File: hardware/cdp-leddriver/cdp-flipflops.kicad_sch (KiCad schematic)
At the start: 9 parts

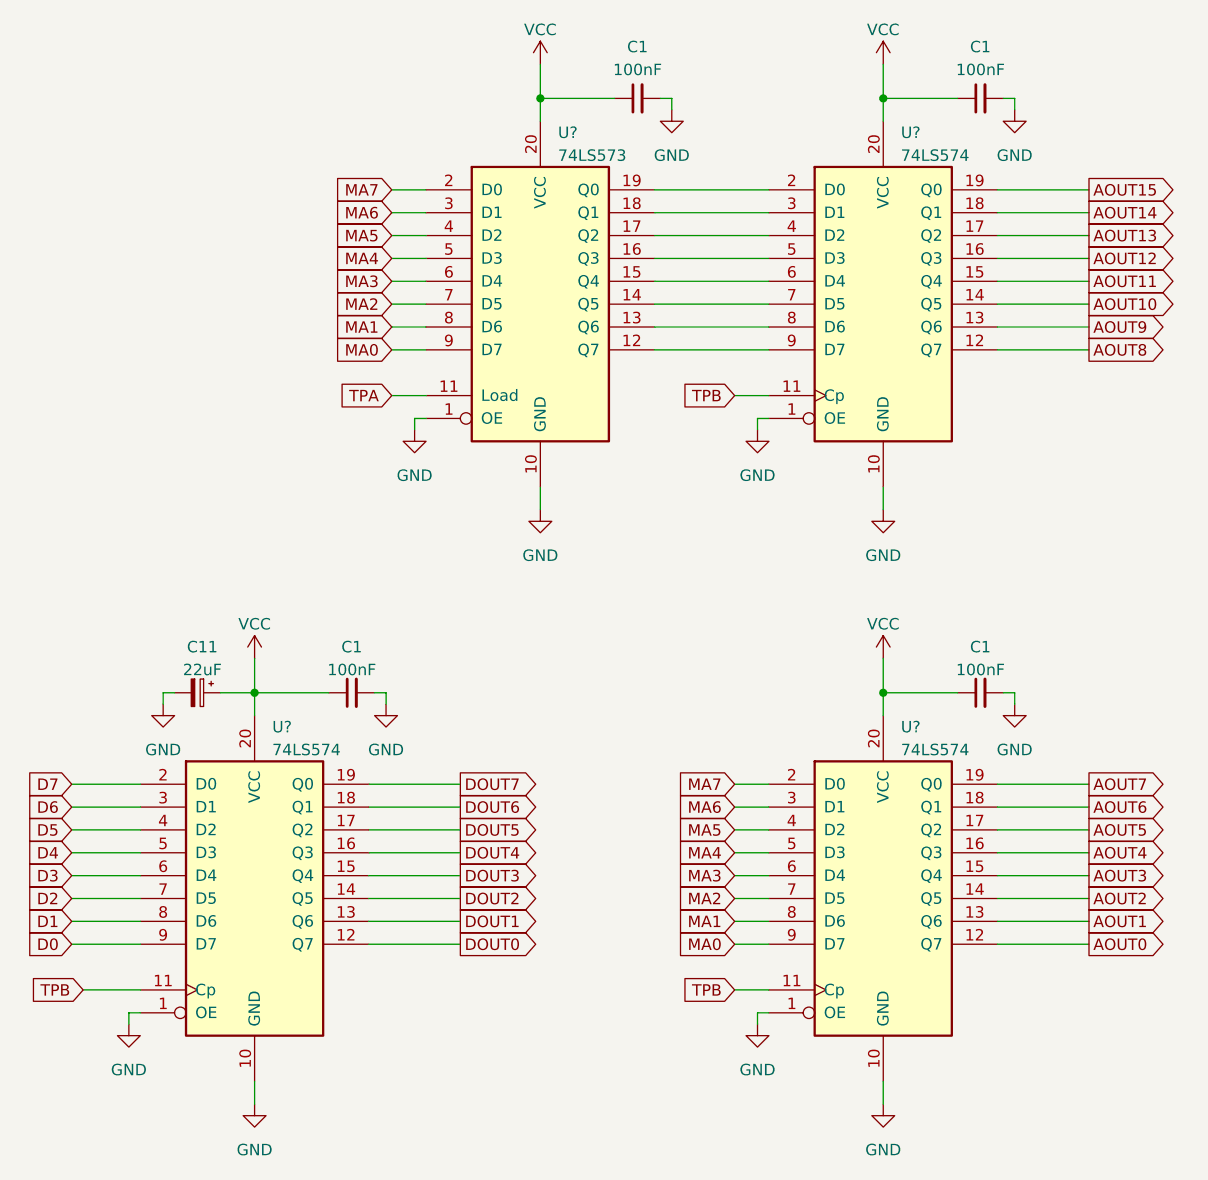
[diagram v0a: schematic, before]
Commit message: IC names fixed on the led driver schematic, on the PCB the MA8-MA15 labels were misaligned that is also fixed. Updated the gerber files.
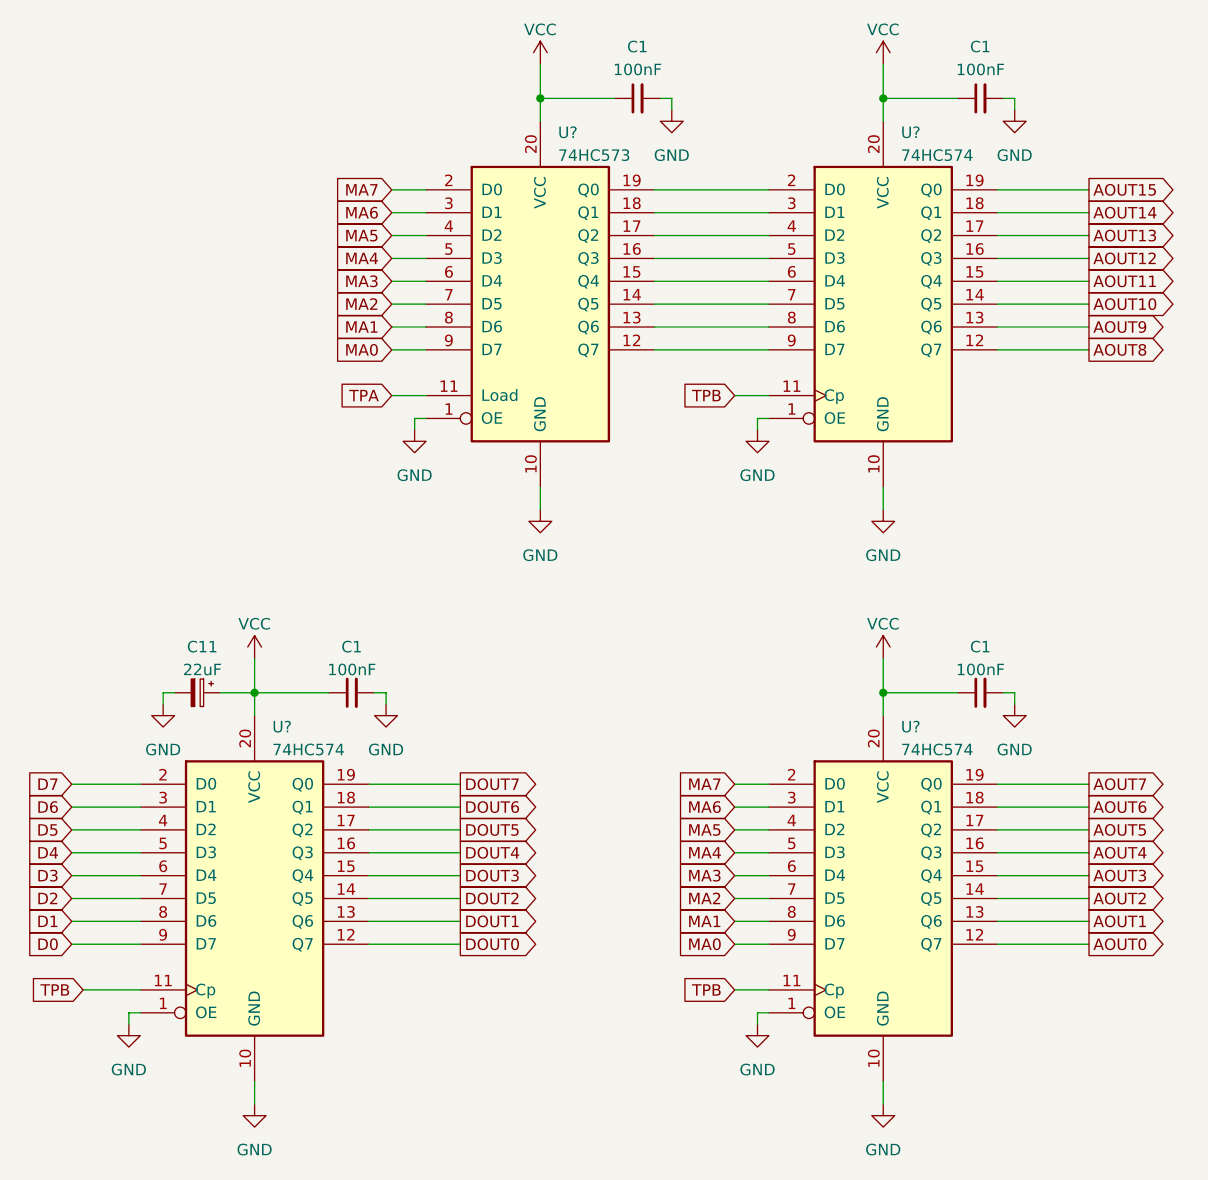
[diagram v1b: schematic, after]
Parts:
- U? (x3): value 74LS574 -> 74HC574
- U?: value 74LS573 -> 74HC573
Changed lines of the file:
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@@
       (effects (font (size 1.27 1.27)) (justify left))
     )
-    (property "Value" "74LS574" (at 197.5359 39.37 0)
+    (property "Value" "74HC574" (at 197.5359 39.37 0)
       (effects (font (size 1.27 1.27)) (justify left))
     )
@@
       (effects (font (size 1.27 1.27)) (justify left))
     )
-    (property "Value" "74LS574" (at 197.5359 105.41 0)
+    (property "Value" "74HC574" (at 197.5359 105.41 0)
       (effects (font (size 1.27 1.27)) (justify left))
     )
@@
       (effects (font (size 1.27 1.27)) (justify left))
     )
-    (property "Value" "74LS574" (at 127.6859 105.41 0)
+    (property "Value" "74HC574" (at 127.6859 105.41 0)
       (effects (font (size 1.27 1.27)) (justify left))
     )
@@
       (effects (font (size 1.27 1.27)) (justify left))
     )
-    (property "Value" "74LS573" (at 159.4359 39.37 0)
-      (effects (font (size 1.27 1.27)) (justify left))
-    )
+    (property "Value" "74HC573" (at 159.4359 39.37 0)
+      (effects (font (size 1.27 1.27)) (justify left))
+    )
